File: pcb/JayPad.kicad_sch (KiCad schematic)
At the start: 26 parts, among them M1 MOUDLE-SEEEDUINO-XIAO, SW1 PEC11-4215F-S24

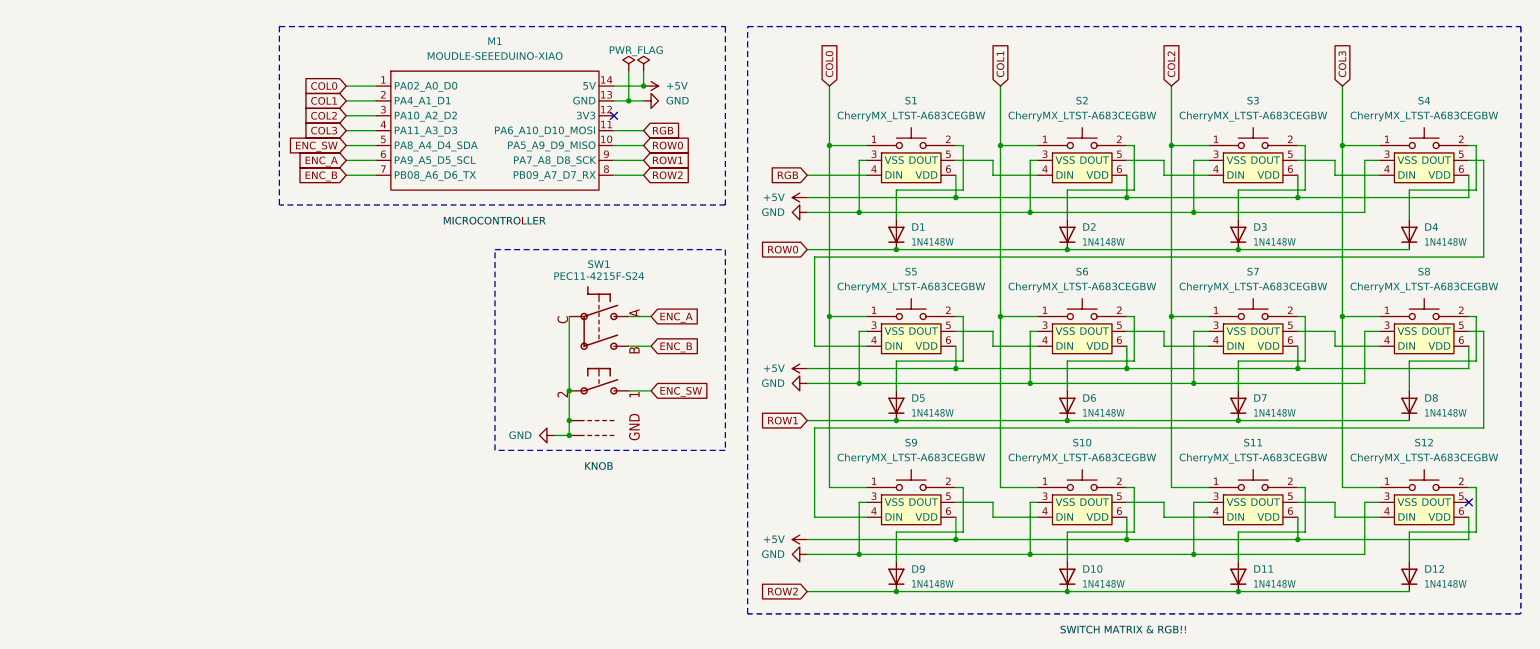
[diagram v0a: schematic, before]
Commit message: Changed from RGB backlight to underglow
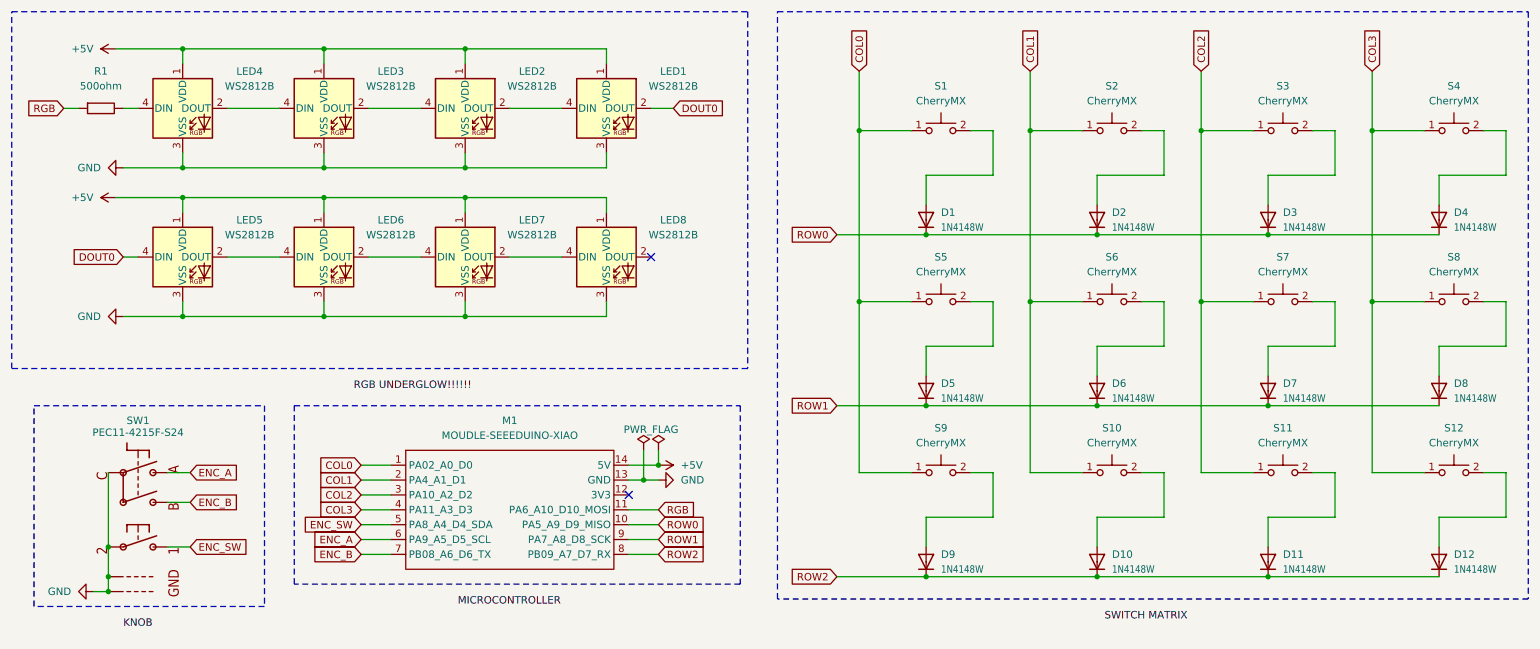
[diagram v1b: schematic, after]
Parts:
- added LED1, LED2, LED3, LED4, LED5, LED6, LED7, LED8: WS2812B, LED_SMD:LED_WS2812B_PLCC4_5.0x5.0mm_P3.2mm, symbol LED:WS2812B
- added R1: 500ohm, Resistor_THT:R_Axial_DIN0207_L6.3mm_D2.5mm_P10.16mm_Horizontal, symbol PCM_SL_Resistors:0ohm
- S1, S10, S11, S12, S2, S3, S4, S5, S6, S7, S8, S9: value CherryMX_LTST-A683CEGBW -> CherryMX; footprint JayPad:CherryMX_1.00u_KailhSocket_LTST-A683CEGBW-HS -> JayPad:CherryMX_1.00u_KailhSocket; symbol CherryMX:CherryMX_LTST-A683CEGBW -> CherryMX:CherryMX
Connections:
- net +5V: now also LED1.1 (VDD), LED2.1 (VDD), LED3.1 (VDD), LED4.1 (VDD), LED5.1 (VDD), LED6.1 (VDD), LED7.1 (VDD), LED8.1 (VDD); no longer S1.6 (VDD), S10.6 (VDD), S11.6 (VDD), S12.6 (VDD), S2.6 (VDD), S3.6 (VDD), S4.6 (VDD), S5.6 (VDD), S6.6 (VDD), S7.6 (VDD), S8.6 (VDD), S9.6 (VDD)
- net GND: now also LED1.3 (VSS), LED2.3 (VSS), LED3.3 (VSS), LED4.3 (VSS), LED5.3 (VSS), LED6.3 (VSS), LED7.3 (VSS), LED8.3 (VSS); no longer S1.3 (VSS), S10.3 (VSS), S11.3 (VSS), S12.3 (VSS), S2.3 (VSS), S3.3 (VSS), S4.3 (VSS), S5.3 (VSS), S6.3 (VSS), S7.3 (VSS), S8.3 (VSS), S9.3 (VSS)
- net RGB: now also R1.1; no longer S1.4 (DIN)
- new net: LED3.4 (DIN), LED4.2 (DOUT)
- new net: LED4.4 (DIN), R1.2
- new net: LED2.4 (DIN), LED3.2 (DOUT)
- new net: LED6.2 (DOUT), LED7.4 (DIN)
- new net: LED5.2 (DOUT), LED6.4 (DIN)
- new net: LED1.4 (DIN), LED2.2 (DOUT)
- new net: LED7.2 (DOUT), LED8.4 (DIN)
- new net DOUT0: LED1.2 (DOUT), LED5.4 (DIN)
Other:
- moved on the sheet: D1, D10, D11, D12, D2, D3, D4, D5, D6, D7, D8, D9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
